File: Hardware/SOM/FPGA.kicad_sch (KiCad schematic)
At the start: 40 parts, among them U1 LFE5UM5G-85F

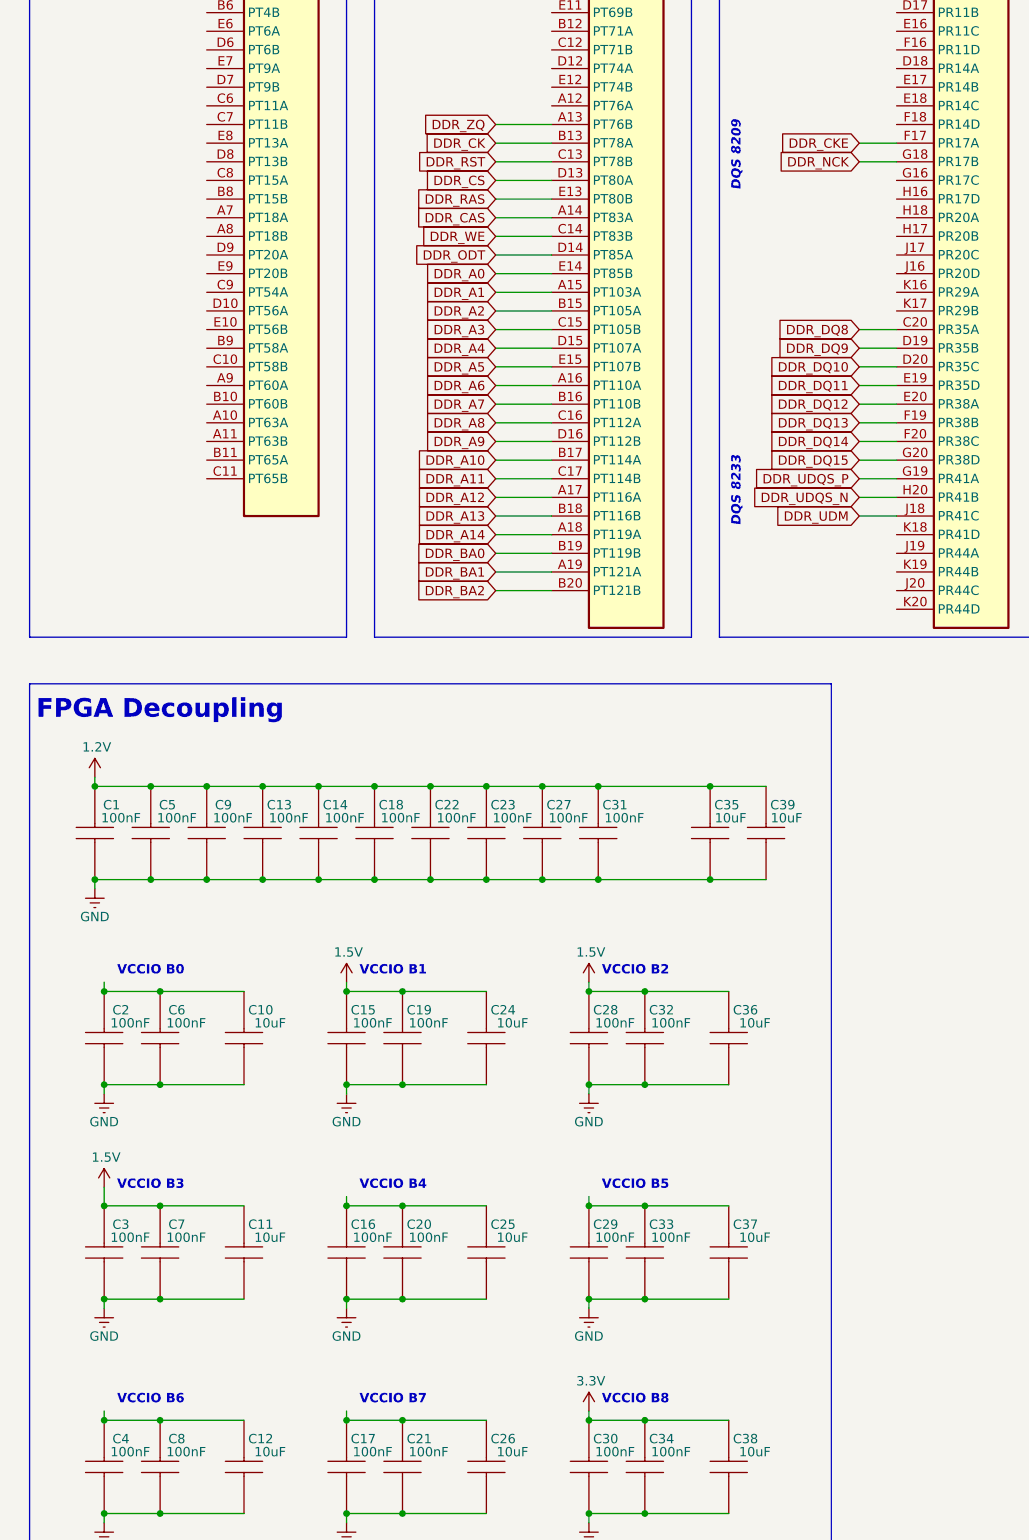
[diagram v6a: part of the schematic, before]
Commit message: DDR clock termination
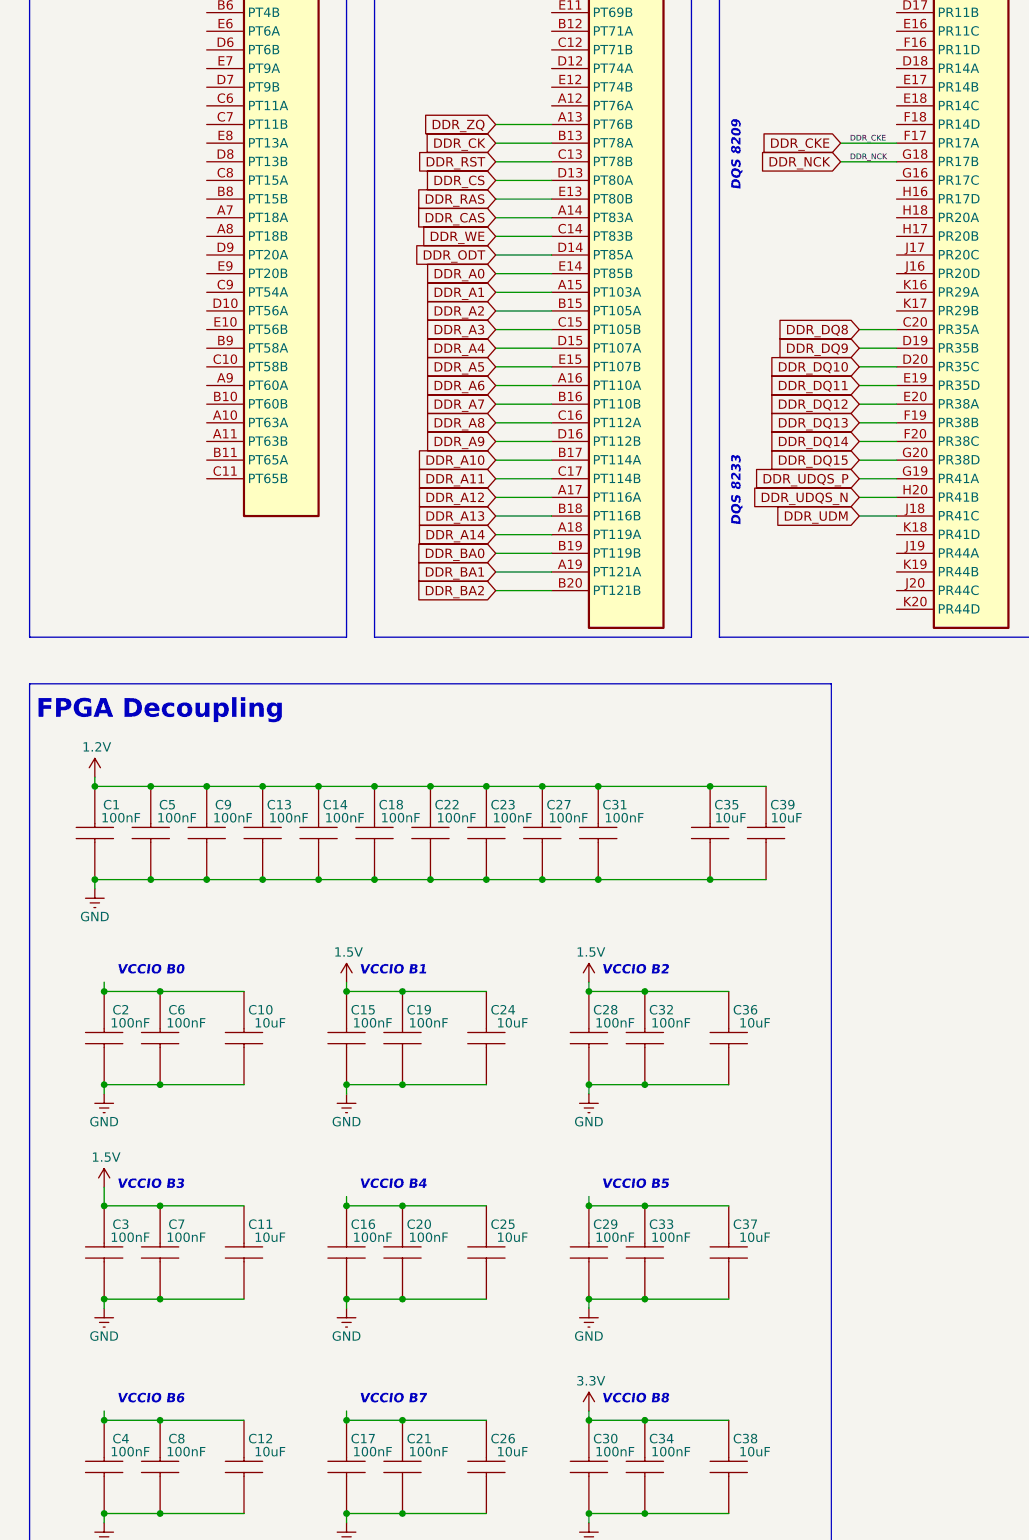
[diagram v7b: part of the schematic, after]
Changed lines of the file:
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@@
-				(thickness 0.254)
-				(bold yes)
-				(color 0 0 132 1)
-			)
-		)
-	)
-	(text "FPGA: BANK-2"
-		(exclude_from_sim no)
-		(at 122.428 23.876 0)
-		(effects
-			(font
-				(size 1.905 1.905)
-				(thickness 0.254)
-				(bold yes)
-			)
-		)
-	)
-	(text "VCCIO B5"
-		(exclude_from_sim no)
-		(at 99.06 205.486 0)
-		(effects
-			(font
-				(size 1.27 1.27)
-				(thickness 0.254)
-				(bold yes)
-				(color 0 0 132 1)
-			)
-		)
-	)
-	(text "FPGA: BANK-0"
-		(exclude_from_sim no)
-		(at 28.194 23.114 0)
-		(effects
-			(font
-				(size 1.905 1.905)
-				(thickness 0.254)
-				(bold yes)
-			)
-		)
-	)
-	(text "FPGA: BANK-7"
-		(exclude_from_sim no)
-		(at 260.858 23.368 0)
-		(effects
-			(font
-				(size 1.905 1.905)
-				(thickness 0.254)
-				(bold yes)
-			)
-		)
-	)
-	(text "FPGA: DEBUG"
-		(exclude_from_sim no)
-		(at 352.044 23.622 0)
-		(effects
-			(font
-				(size 1.905 1.905)
-				(thickness 0.254)
-				(bold yes)
-			)
-		)
-	)
-	(text "DQS 8209"
-		(exclude_from_sim no)
-		(at 112.776 65.278 90)
-		(effects
-			(font
-				(size 1.27 1.27)
 				(thickness 0.254)
 				(bold yes)
@@
 		)
 	)
-	(text "VCCIO B7"
+	(text "FPGA: BANK-2"
 		(exclude_from_sim no)
-		(at 66.04 234.696 0)
-		(effects
-			(font
-				(size 1.27 1.27)
+		(at 122.428 23.876 0)
+		(effects
+			(font
+				(size 1.905 1.905)
 				(thickness 0.254)
 				(bold yes)
-				(color 0 0 132 1)
-			)
-		)
-	)
-	(text "VCCIO B4"
+			)
+		)
+	)
+	(text "VCCIO B5"
 		(exclude_from_sim no)
-		(at 66.04 205.486 0)
-		(effects
-			(font
-				(size 1.27 1.27)
-				(thickness 0.254)
-				(bold yes)
-				(color 0 0 132 1)
-			)
-		)
-	)
-	(text "DQS 8281"
-		(exclude_from_sim no)
-		(at 159.258 108.712 90)
+		(at 99.06 205.486 0)
 		(effects
 			(font
@@
 		)
 	)
-	(text "VCCIO B6"
+	(text "FPGA: BANK-0"
 		(exclude_from_sim no)
-		(at 33.02 234.696 0)
-		(effects
-			(font
-				(size 1.27 1.27)
+		(at 28.194 23.114 0)
+		(effects
+			(font
+				(size 1.905 1.905)
 				(thickness 0.254)
 				(bold yes)
-				(color 0 0 132 1)
-			)
-		)
-	)
-	(text "VCCIO B1"
+			)
+		)
+	)
+	(text "FPGA: BANK-7"
 		(exclude_from_sim no)
-		(at 66.04 176.276 0)
-		(effects
-			(font
-				(size 1.27 1.27)
+		(at 260.858 23.368 0)
+		(effects
+			(font
+				(size 1.905 1.905)
 				(thickness 0.254)
 				(bold yes)
-				(color 0 0 132 1)
-			)
-		)
-	)
-	(text "VCCIO B0"
+			)
+		)
+	)
+	(text "FPGA: DEBUG"
 		(exclude_from_sim no)
-		(at 33.02 176.276 0)
-		(effects
-			(font
-				(size 1.27 1.27)
+		(at 352.044 23.622 0)
+		(effects
+			(font
+				(size 1.905 1.905)
 				(thickness 0.254)
 				(bold yes)
-				(color 0 0 132 1)
-			)
-		)
-	)
-	(text "DQS 8233"
+			)
+		)
+	)
+	(text "DQS 8209"
 		(exclude_from_sim no)
-		(at 112.776 110.998 90)
+		(at 112.776 65.278 90)
 		(effects
 			(font
@@
 		)
 	)
+	(text "VCCIO B7"
+		(exclude_from_sim no)
+		(at 66.04 234.696 0)
+		(effects
+			(font
+				(size 1.27 1.27)
+				(thickness 0.254)
+				(bold yes)
+				(italic yes)
+				(color 0 132 0 1)
+			)
+		)
+	)
+	(text "VCCIO B4"
+		(exclude_from_sim no)
+		(at 66.04 205.486 0)
+		(effects
+			(font
+				(size 1.27 1.27)
+				(thickness 0.254)
+				(bold yes)
+				(italic yes)
+				(color 0 132 0 1)
+			)
+		)
+	)
+	(text "DQS 8281"
+		(exclude_from_sim no)
+		(at 159.258 108.712 90)
+		(effects
+			(font
+				(size 1.27 1.27)
+				(thickness 0.254)
+				(bold yes)
+				(italic yes)
+				(color 0 132 0 1)
+			)
+		)
+	)
+	(text "VCCIO B6"
+		(exclude_from_sim no)
+		(at 33.02 234.696 0)
+		(effects
+			(font
+				(size 1.27 1.27)
+				(thickness 0.254)
+				(bold yes)
+				(italic yes)
+				(color 0 132 0 1)
+			)
+		)
+	)
+	(text "VCCIO B1"
+		(exclude_from_sim no)
+		(at 66.04 176.276 0)
+		(effects
+			(font
+				(size 1.27 1.27)
+				(thickness 0.254)
+				(bold yes)
+				(italic yes)
+				(color 0 132 0 1)
+			)
+		)
+	)
+	(text "VCCIO B0"
+		(exclude_from_sim no)
+		(at 33.02 176.276 0)
+		(effects
+			(font
+				(size 1.27 1.27)
+				(thickness 0.254)
+				(bold yes)
+				(italic yes)
+				(color 0 132 0 1)
+			)
+		)
+	)
+	(text "DQS 8233"
+		(exclude_from_sim no)
+		(at 112.776 110.998 90)
+		(effects
+			(font
+				(size 1.27 1.27)
+				(thickness 0.254)
+				(bold yes)
+				(italic yes)
+				(color 0 132 0 1)
+			)
+		)
+	)
 	(text "VCCIO B3"
 		(exclude_from_sim no)
@@
 				(thickness 0.254)
 				(bold yes)
-				(color 0 0 132 1)
+				(italic yes)
+				(color 0 132 0 1)
 			)
 		)
@@
 				(thickness 0.254)
 				(bold yes)
-				(color 0 0 132 1)
+				(italic yes)
+				(color 0 132 0 1)
 			)
 		)
@@
 	(wire
 		(pts
-			(xy 129.54 63.5) (xy 134.62 63.5)
+			(xy 127 63.5) (xy 134.62 63.5)
 		)
 		(stroke
@@
 	(wire
 		(pts
-			(xy 129.54 66.04) (xy 134.62 66.04)
+			(xy 127 66.04) (xy 134.62 66.04)
 		)
 		(stroke
@@
 		)
 	)
+	(label "DDR_NCK"
+		(at 128.27 66.04 0)
+		(effects
+			(font
+				(size 0.762 0.762)
+			)
+			(justify left bottom)
+		)
+	)
+	(label "DDR_CKE"
+		(at 128.27 63.5 0)
+		(effects
+			(font
+				(size 0.762 0.762)
+			)
+			(justify left bottom)
+		)
+	)
 	(global_label "DDR_A14"
 		(shape input)
@@
 	(global_label "DDR_CKE"
 		(shape input)
-		(at 129.54 63.5 180)
-		(fields_autoplaced yes)
-		(effects
-			(font
-				(size 1.27 1.27)
-			)
-			(justify right)
-		)
-		(property "Intersheetrefs" "${INTERSHEET_REFS}"
-			(at 118.0882 63.5 0)
+		(at 127 63.5 180)
+		(fields_autoplaced yes)
+		(effects
+			(font
+				(size 1.27 1.27)
+			)
+			(justify right)
+		)
+		(property "Intersheetrefs" "${INTERSHEET_REFS}"
+			(at 115.5482 63.5 0)
 			(effects
 				(font
@@
 	(global_label "DDR_NCK"
 		(shape input)
-		(at 129.54 66.04 180)
-		(fields_autoplaced yes)
-		(effects
-			(font
-				(size 1.27 1.27)
-			)
-			(justify right)
-		)
-		(property "Intersheetrefs" "${INTERSHEET_REFS}"
-			(at 117.9067 66.04 0)
-			(effects
-				(font
+		(at 127 66.04 180)
+		(fields_autoplaced yes)
+		(effects
+			(font
+				(size 1.27 1.27)
+			)
+			(justify right)
+		)
+		(property "Intersheetrefs" "${INTERSHEET_REFS}"
+			(at 115.3667 66.04 0)
+			(effects
+				(font

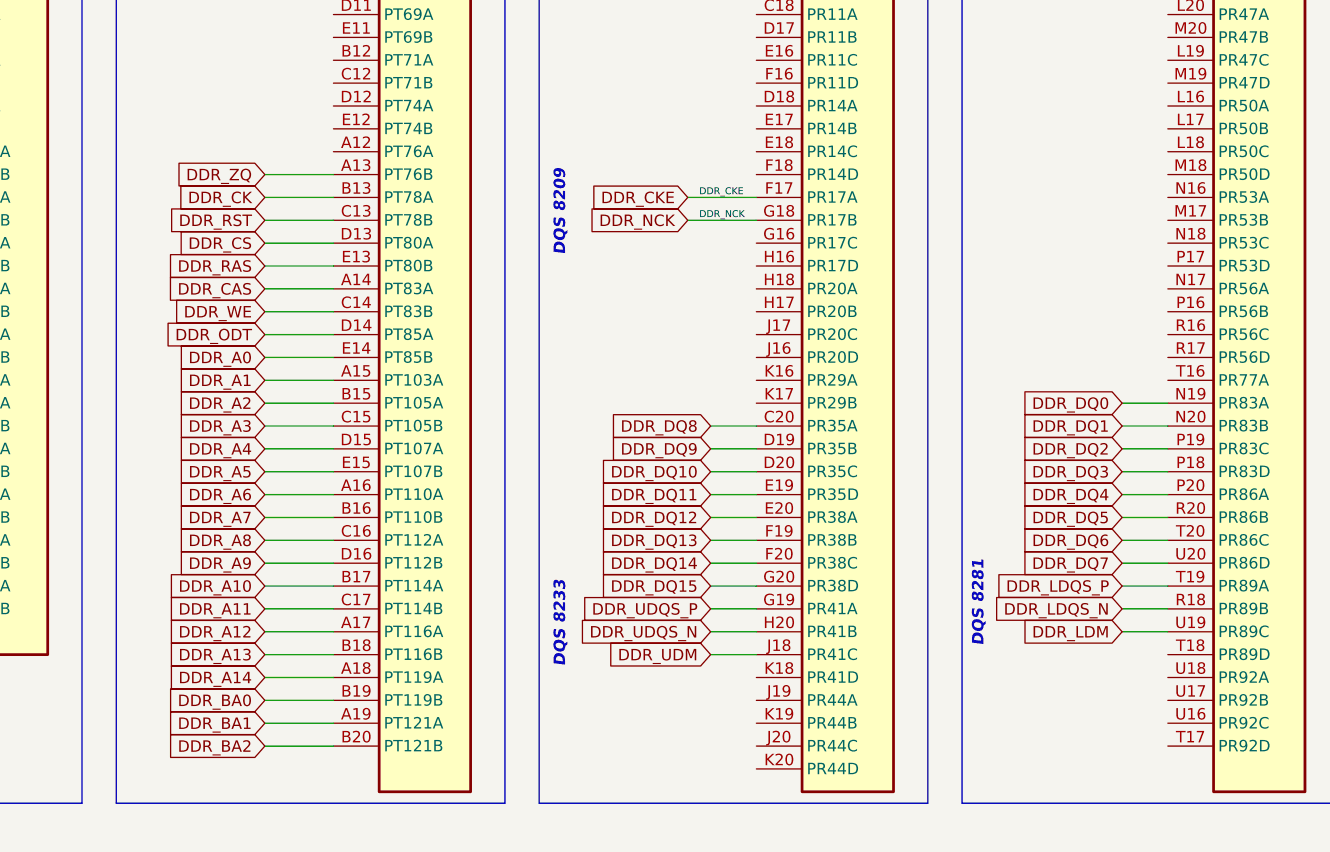
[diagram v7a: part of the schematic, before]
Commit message: ZQ calibration resistor added
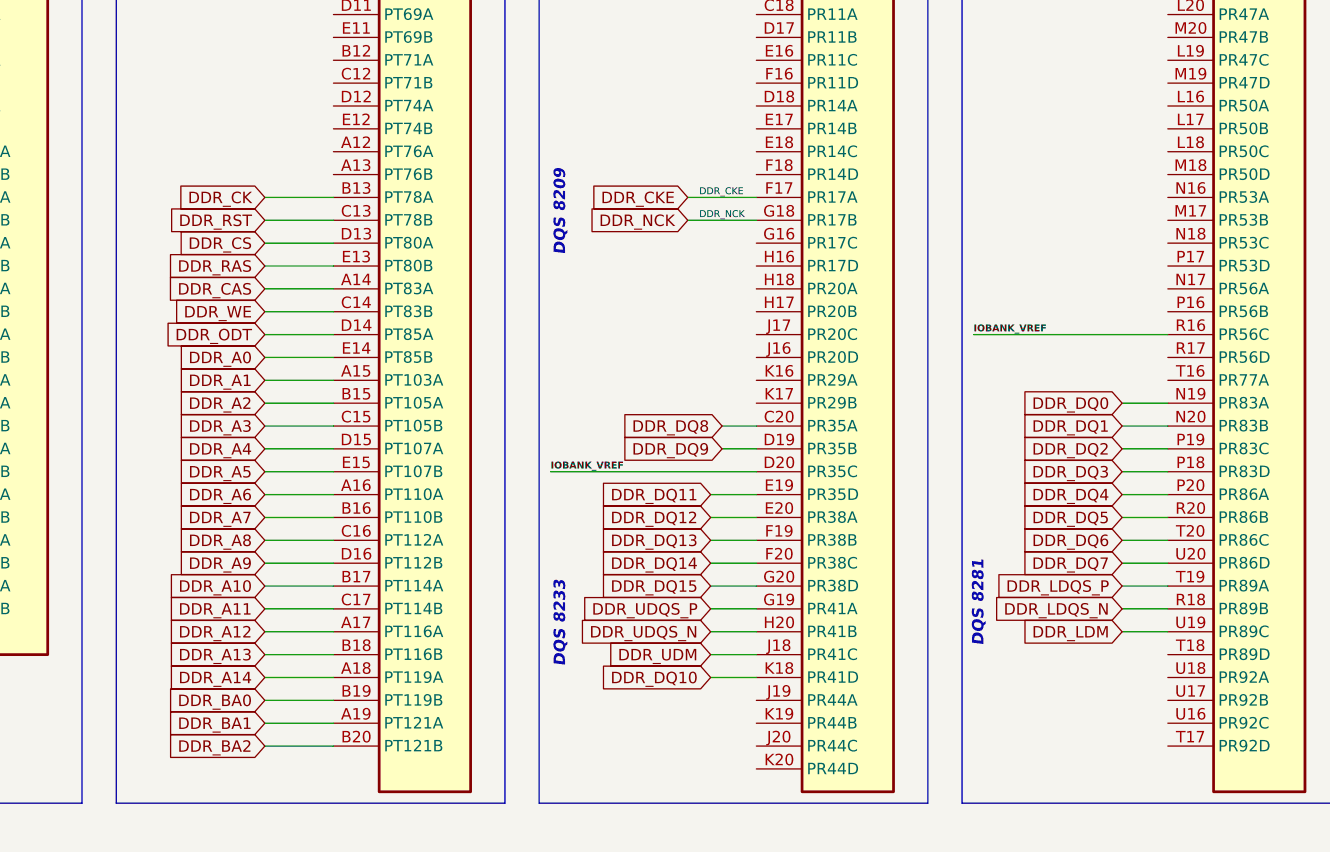
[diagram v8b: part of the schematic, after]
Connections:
- net DDR_DQ10: now also U1.K18 (PR41D); no longer U1.D20 (PR35C)
- net IOBANK_VREF: now reaches U1.R16 (PR56C)
- net IOBANK_VREF: now also U1.D20 (PR35C)
- net DDR_ZQ: no longer names the net of U1.A13 (PT76B)
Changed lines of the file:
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@@
-	(wire
-		(pts
-			(xy 129.54 93.98) (xy 134.62 93.98)
-		)
-		(stroke
-			(width 0)
-			(type default)
-		)
-	)
 	(wire
 		(pts
@@
 	(wire
 		(pts
-			(xy 129.54 91.44) (xy 134.62 91.44)
+			(xy 130.81 91.44) (xy 134.62 91.44)
 		)
 		(stroke
@@
 	(wire
 		(pts
+			(xy 158.75 78.74) (xy 180.34 78.74)
+		)
+		(stroke
+			(width 0)
+			(type default)
+		)
+	)
+	(wire
+		(pts
 			(xy 129.54 101.6) (xy 134.62 101.6)
 		)
@@
 	(wire
 		(pts
+			(xy 129.54 116.84) (xy 134.62 116.84)
+		)
+		(stroke
+			(width 0)
+			(type default)
+		)
+	)
+	(wire
+		(pts
 			(xy 55.88 163.83) (xy 63.5 163.83)
 		)
@@
 	(wire
 		(pts
-			(xy 80.01 60.96) (xy 87.63 60.96)
-		)
-		(stroke
-			(width 0)
-			(type default)
-		)
-	)
-	(wire
-		(pts
 			(xy 86.36 163.83) (xy 93.98 163.83)
 		)
@@
 	(wire
 		(pts
-			(xy 129.54 88.9) (xy 134.62 88.9)
+			(xy 130.81 88.9) (xy 134.62 88.9)
 		)
 		(stroke
@@
 		(pts
 			(xy 59.69 191.77) (xy 59.69 193.04)
+		)
+		(stroke
+			(width 0)
+			(type default)
+		)
+	)
+	(wire
+		(pts
+			(xy 111.76 93.98) (xy 134.62 93.98)
 		)
 		(stroke
@@
 		)
 	)
+	(label "IOBANK_VREF"
+		(at 111.76 93.98 0)
+		(effects
+			(font
+				(size 0.762 0.762)
+				(thickness 0.1524)
+				(bold yes)
+			)
+			(justify left bottom)
+		)
+	)
 	(label "DDR_CKE"
 		(at 128.27 63.5 0)
@@
 		)
 	)
+	(label "IOBANK_VREF"
+		(at 158.75 78.74 0)
+		(effects
+			(font
+				(size 0.762 0.762)
+				(thickness 0.1524)
+				(bold yes)
+			)
+			(justify left bottom)
+		)
+	)
 	(global_label "DDR_A14"
 		(shape input)
@@
 	(global_label "DDR_DQ10"
 		(shape input)
-		(at 129.54 93.98 180)
-		(fields_autoplaced yes)
-		(effects
-			(font
-				(size 1.27 1.27)
-			)
-			(justify right)
-		)
-		(property "Intersheetrefs" "${INTERSHEET_REFS}"
-			(at 116.7577 93.98 0)
+		(at 129.54 116.84 180)
+		(fields_autoplaced yes)
+		(effects
+			(font
+				(size 1.27 1.27)
+				(thickness 0.1588)
+			)
+			(justify right)
+		)
+		(property "Intersheetrefs" "${INTERSHEET_REFS}"
+			(at 116.7577 116.84 0)
 			(effects
 				(font
@@
 	(global_label "DDR_DQ8"
 		(shape input)
-		(at 129.54 88.9 180)
-		(fields_autoplaced yes)
-		(effects
-			(font
-				(size 1.27 1.27)
-			)
-			(justify right)
-		)
-		(property "Intersheetrefs" "${INTERSHEET_REFS}"
-			(at 117.9672 88.9 0)
+		(at 130.81 88.9 180)
+		(fields_autoplaced yes)
+		(effects
+			(font
+				(size 1.27 1.27)
+			)
+			(justify right)
+		)
+		(property "Intersheetrefs" "${INTERSHEET_REFS}"
+			(at 119.2372 88.9 0)
 			(effects
 				(font
@@
 		)
 	)
-	(global_label "DDR_ZQ"
-		(shape input)
-		(at 80.01 60.96 180)
-		(fields_autoplaced yes)
-		(effects
-			(font
-				(size 1.27 1.27)
-			)
-			(justify right)
-		)
-		(property "Intersheetrefs" "${INTERSHEET_REFS}"
-			(at 69.7072 60.96 0)
-			(effects
-				(font
-					(size 1.27 1.27)
-				)
-				(justify right)
-				(hide yes)
-			)
-		)
-	)
 	(global_label "DDR_RST"
 		(shape input)
@@
 	(global_label "DDR_DQ9"
 		(shape input)
-		(at 129.54 91.44 180)
-		(fields_autoplaced yes)
-		(effects
-			(font
-				(size 1.27 1.27)
-			)
-			(justify right)
-		)
-		(property "Intersheetrefs" "${INTERSHEET_REFS}"
-			(at 117.9672 91.44 0)
-			(effects
-				(font
+		(at 130.81 91.44 180)
+		(fields_autoplaced yes)
+		(effects
+			(font
+				(size 1.27 1.27)
+			)
+			(justify right)
+		)
+		(property "Intersheetrefs" "${INTERSHEET_REFS}"
+			(at 119.2372 91.44 0)
+			(effects
+				(font
